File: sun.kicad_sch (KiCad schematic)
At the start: 5 parts, among them IC1 TSL25853PM, IC2 TSL25853PM, IC3 TSL25853PM, IC4 TSL25853PM, IC5 TSL25853PM

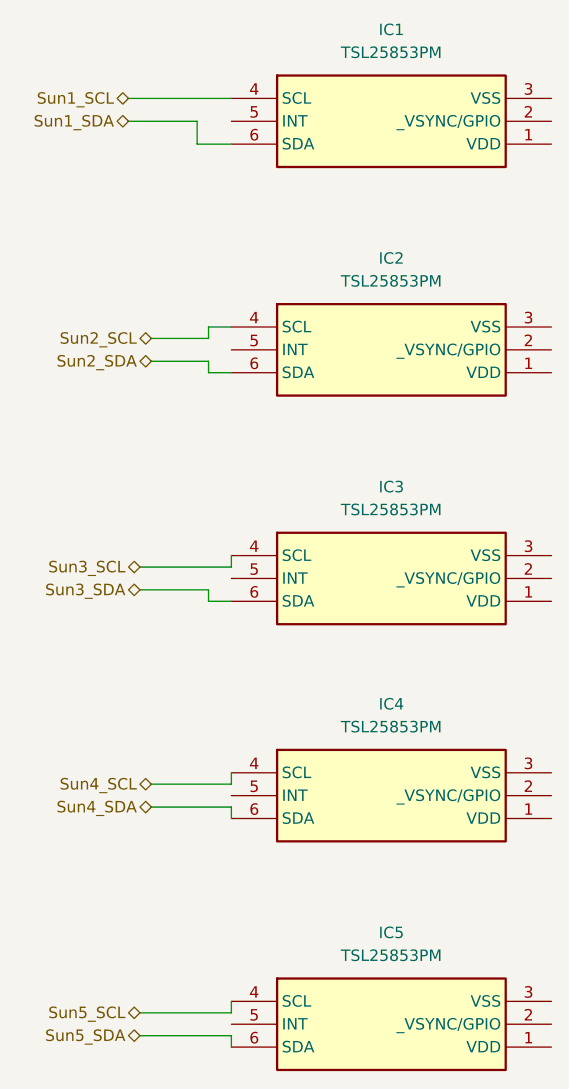
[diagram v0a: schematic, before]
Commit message: Magnetometer fixes\n\nCloses #2
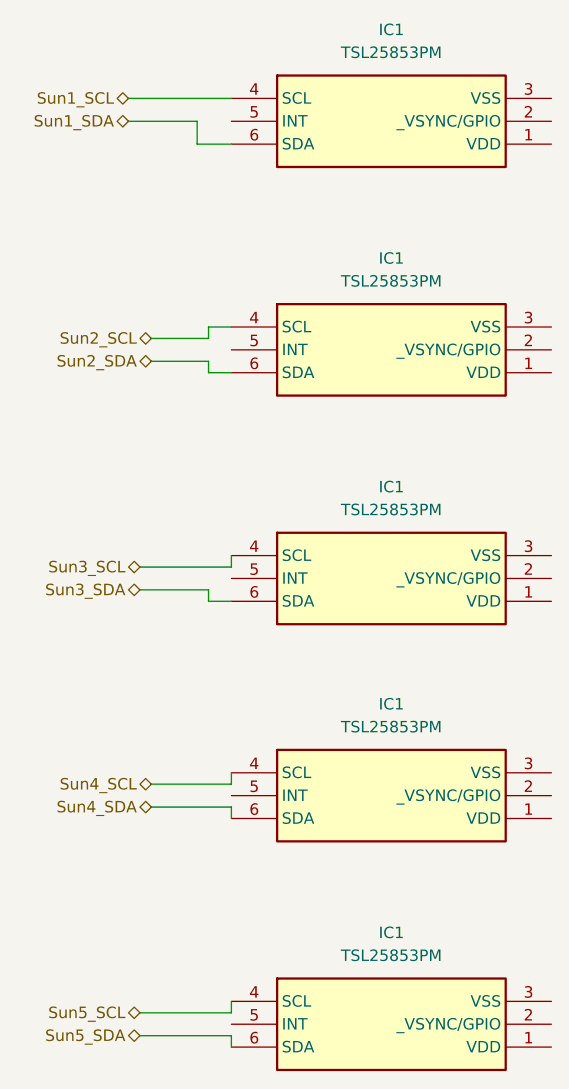
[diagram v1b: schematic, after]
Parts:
- renumbered IC3 to IC1, IC4 to IC1, IC2 to IC1, IC5 to IC1
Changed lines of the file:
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@@
   (symbol (lib_id "TSL25853PM:TSL25853PM") (at 66.04 110.49 0) (unit 1)
     (in_bom yes) (on_board yes) (dnp no) (fields_autoplaced)
-    (property "Reference" "IC3" (at 83.82 102.87 0)
+    (property "Reference" "IC1" (at 83.82 102.87 0)
       (effects (font (size 1.27 1.27)))
     )
@@
   (symbol (lib_id "TSL25853PM:TSL25853PM") (at 66.04 134.62 0) (unit 1)
     (in_bom yes) (on_board yes) (dnp no) (fields_autoplaced)
-    (property "Reference" "IC4" (at 83.82 127 0)
+    (property "Reference" "IC1" (at 83.82 127 0)
       (effects (font (size 1.27 1.27)))
     )
@@
   (symbol (lib_id "TSL25853PM:TSL25853PM") (at 66.04 85.09 0) (unit 1)
     (in_bom yes) (on_board yes) (dnp no) (fields_autoplaced)
-    (property "Reference" "IC2" (at 83.82 77.47 0)
+    (property "Reference" "IC1" (at 83.82 77.47 0)
       (effects (font (size 1.27 1.27)))
     )
@@
   (symbol (lib_id "TSL25853PM:TSL25853PM") (at 66.04 160.02 0) (unit 1)
     (in_bom yes) (on_board yes) (dnp no) (fields_autoplaced)
-    (property "Reference" "IC5" (at 83.82 152.4 0)
-      (effects (font (size 1.27 1.27)))
-    )
+    (property "Reference" "IC1" (at 83.82 152.4 0)
+      (effects (font (size 1.27 1.27)))
+    )
